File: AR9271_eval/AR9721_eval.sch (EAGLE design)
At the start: 135 parts, among them J1 UJ2-MIBH2-4-SMT-TR, J3 HTST-110-01-XX-DV, J7 132134-15, J8 132134-15, U1 U-ATHEROS-AR9271, U2 AT24C04C-XHM-T, U3 LT3080EQPBF, U4 LT3080EQPBF, U5 LT3080EQPBF, U6 LT3080EQPBF, Y1 ECS-400-10-36-CKY-TR

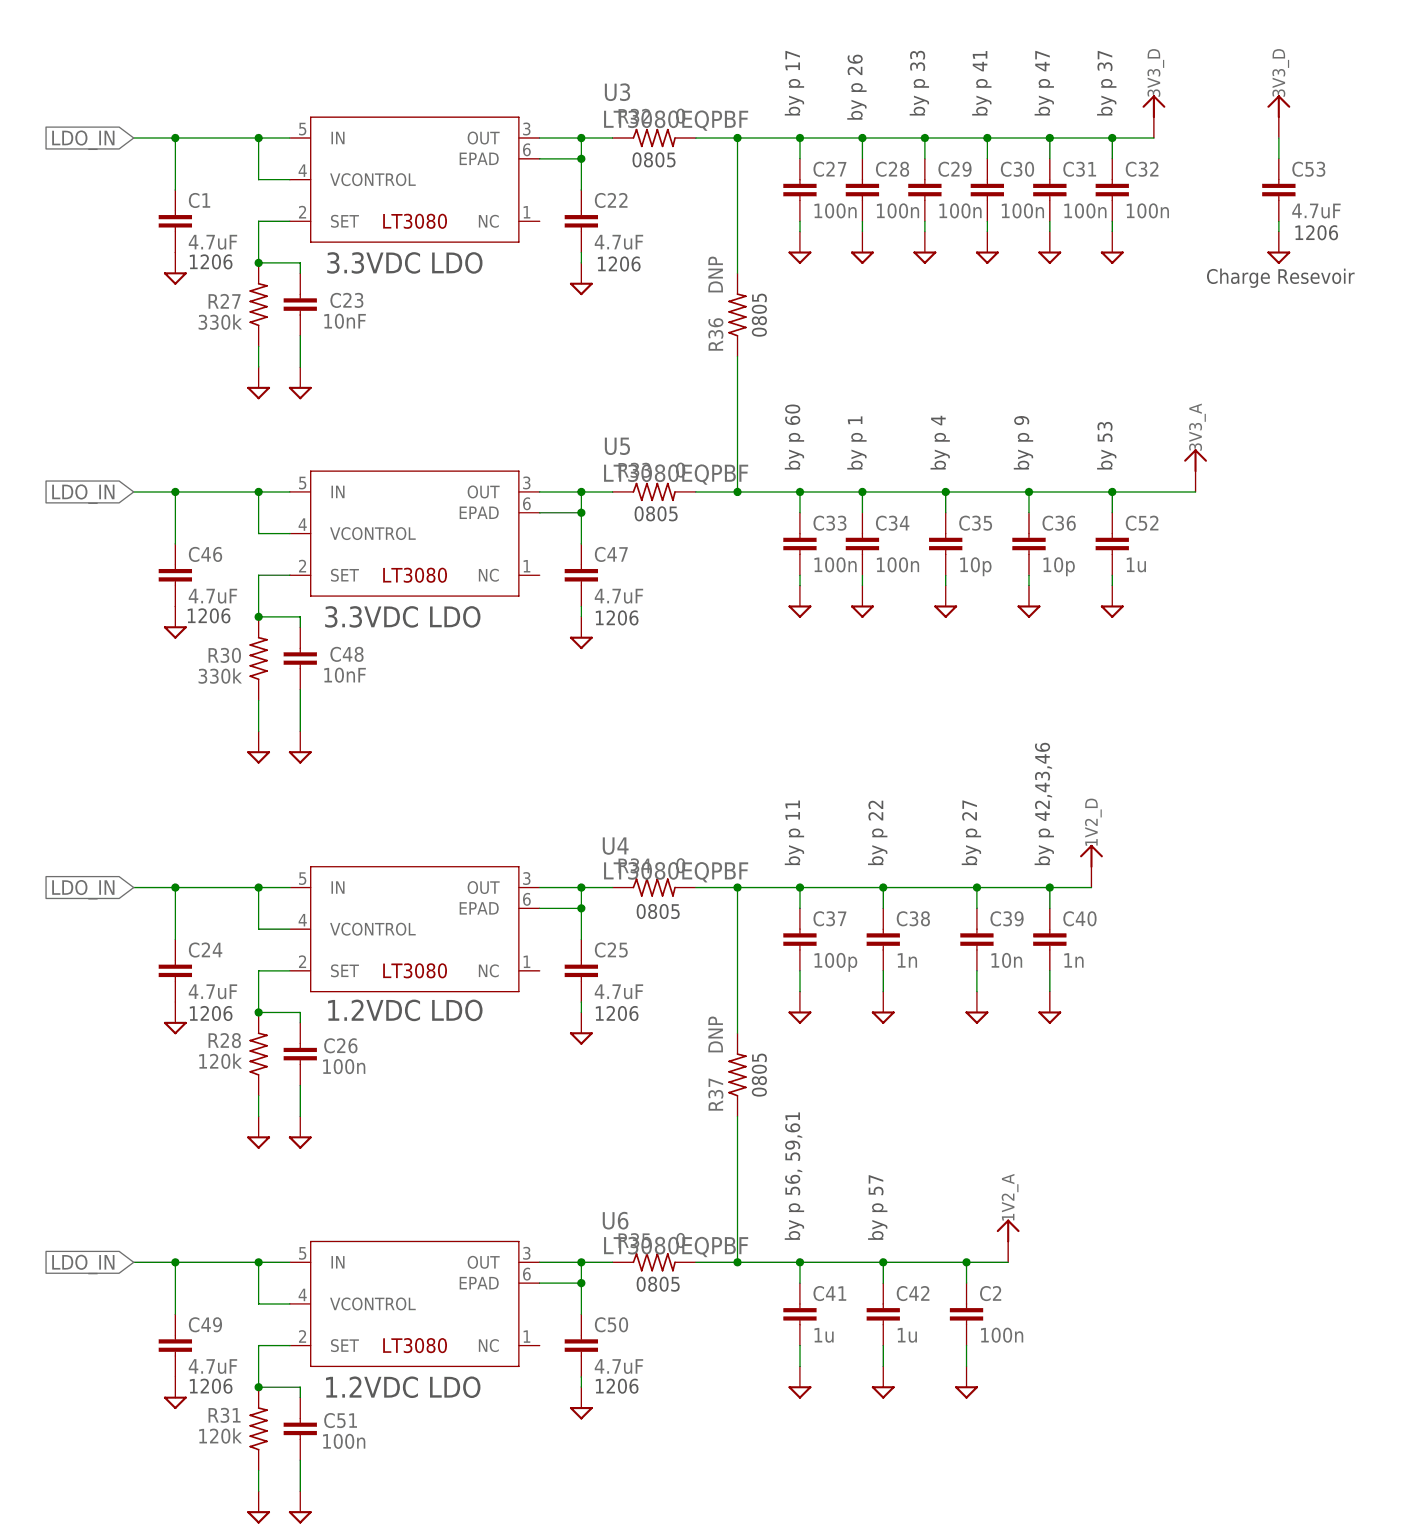
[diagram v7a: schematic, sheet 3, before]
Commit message: Fixed comments on JP4 and moved some names/values around after talking with Glenn.
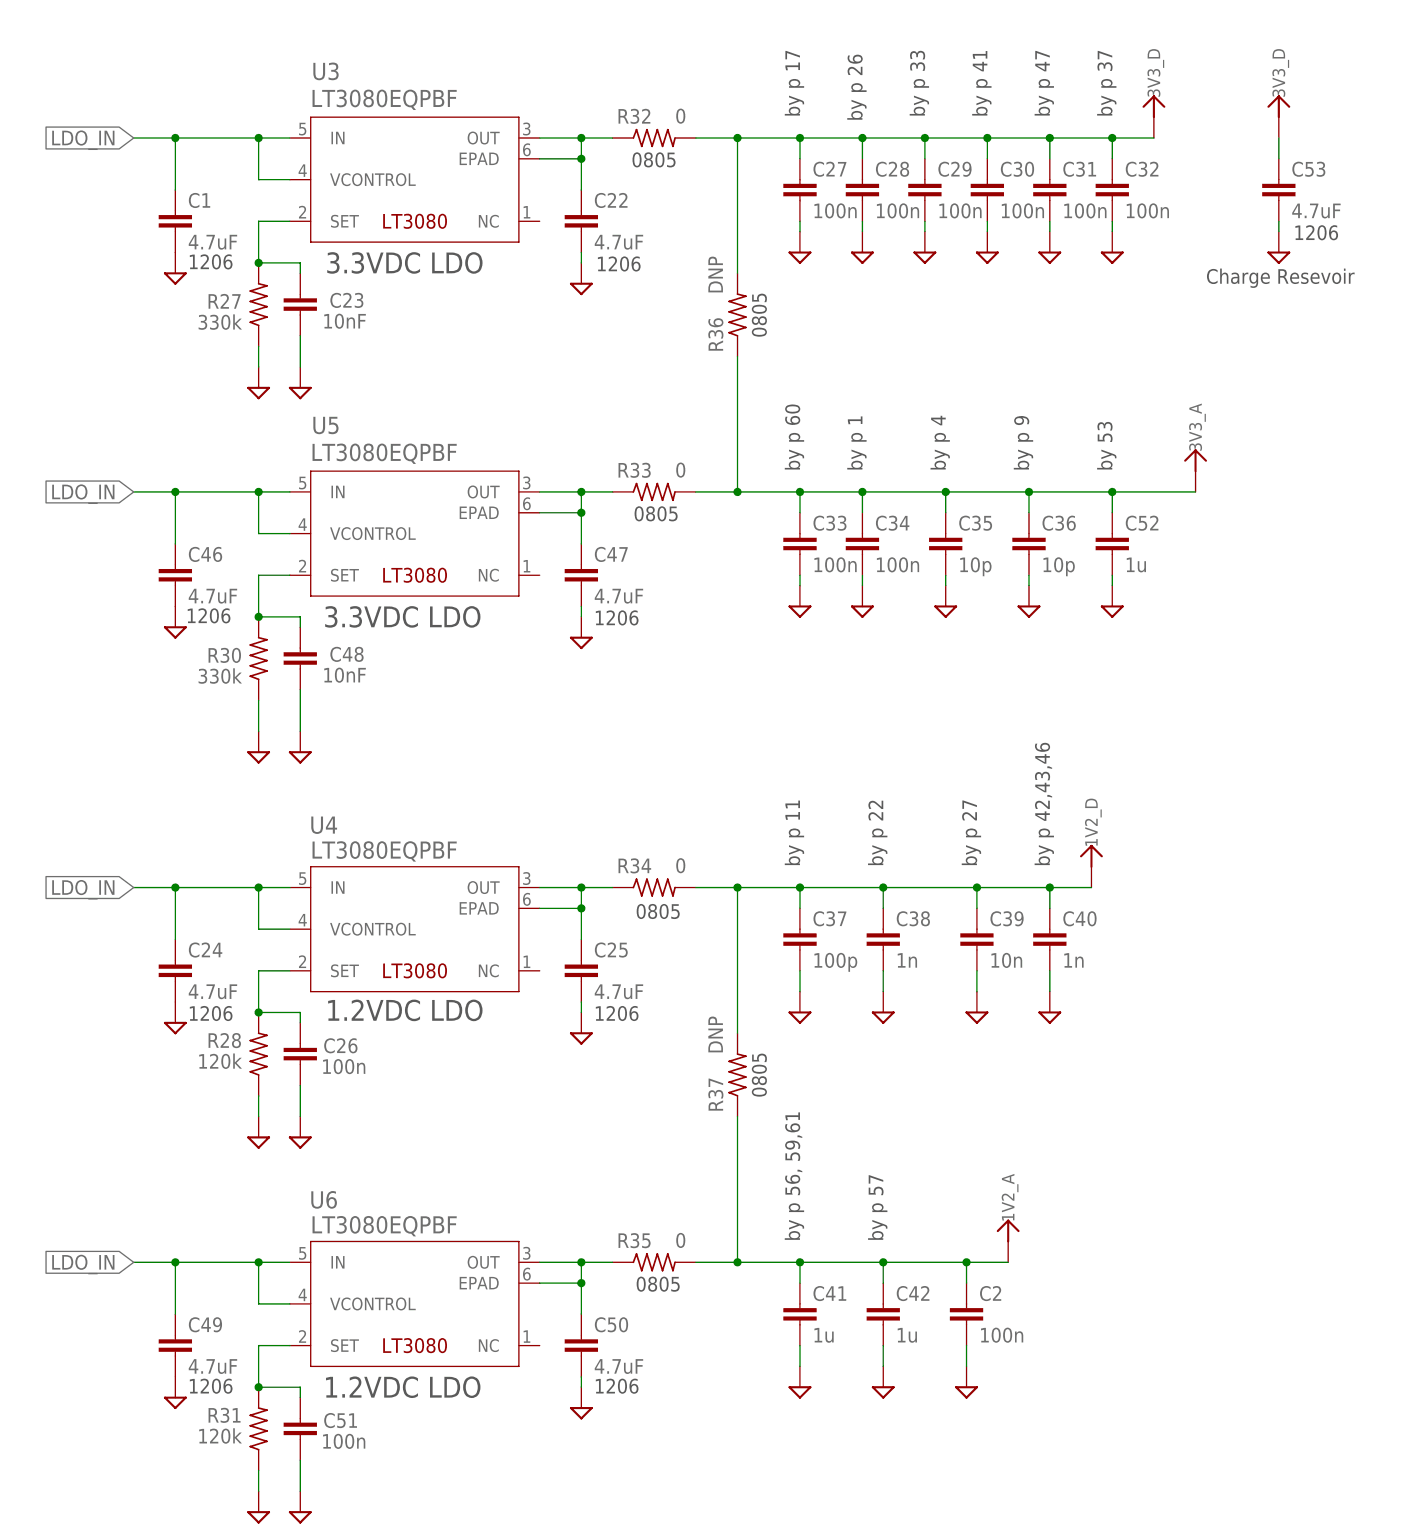
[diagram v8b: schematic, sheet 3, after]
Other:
- note added: "To use USB power for LDO input, connect connect Pin 5 to Pin 6 with jumper clip."
- note added: "To use lab supply, connect +5VDC to Pin 3 and Ground to Pin 7 or 8. Connect Pin 4 to Pin 5 with jumper clip."
- note removed: "To use USB for LDO input, connect connect Pin 3 to Pin 4 with jumper clip."
- note removed: "To use lab supply, connect +5VDC to Pin 6 and Ground to Pin 7 or 8. Connect Pin 5 to Pin 4 with jumper clip."
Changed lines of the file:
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@@
 <setting verticaltext="up"/>
 </settings>
-<grid distance="0.05" unitdist="inch" unit="inch" style="lines" multiple="2" display="no" altdistance="0.01" altunitdist="inch" altunit="inch"/>
+<grid distance="0.1" unitdist="inch" unit="inch" style="lines" multiple="1" display="no" altdistance="0.01" altunitdist="inch" altunit="inch"/>
 <layers>
 <layer number="1" name="Top" color="4" fill="1" visible="no" active="no"/>
@@
 <text x="86.106" y="216.408" size="1.778" layer="97">Ground</text>
 <text x="82.296" y="213.868" size="1.778" layer="97">Lab Supply</text>
-<text x="44.45" y="214.63" size="1.27" layer="97">To use USB for LDO input, connect
-connect Pin 3 to Pin 4 with jumper clip.</text>
-<text x="44.45" y="206.502" size="1.27" layer="97">To use lab supply, connect +5VDC to Pin 6
- and Ground to Pin 7 or 8. Connect Pin 5 to
- Pin 4 with jumper clip.</text>
+<text x="44.45" y="214.63" size="1.27" layer="97">To use USB power for LDO input, connect
+connect Pin 5 to Pin 6 with jumper clip.</text>
+<text x="44.45" y="206.502" size="1.27" layer="97">To use lab supply, connect +5VDC to Pin 3
+ and Ground to Pin 7 or 8. Connect Pin 4 to
+ Pin 5 with jumper clip.</text>
 <text x="302.768" y="132.588" size="1.778" layer="97">Serial Port</text>
 <text x="375.158" y="112.268" size="1.778" layer="97">GPIOs (8)</text>
@@
 </instance>
 <instance part="U3" gate="A" x="69.85" y="182.88" smashed="yes">
-<attribute name="NAME" x="92.8116" y="192.5066" size="2.0828" layer="95" ratio="6" rot="SR0"/>
-<attribute name="VALUE" x="92.6846" y="189.2046" size="2.0828" layer="96" ratio="6" rot="SR0"/>
+<attribute name="NAME" x="57.2516" y="195.0466" size="2.0828" layer="95" ratio="6" rot="SR0"/>
+<attribute name="VALUE" x="57.1246" y="191.7446" size="2.0828" layer="96" ratio="6" rot="SR0"/>
 </instance>
 <instance part="C1" gate="G$1" x="40.64" y="179.07" smashed="yes">
@@
 </instance>
 <instance part="U4" gate="A" x="69.85" y="91.44" smashed="yes">
-<attribute name="NAME" x="92.5576" y="100.5586" size="2.0828" layer="95" ratio="6" rot="SR0"/>
-<attribute name="VALUE" x="92.6846" y="97.5106" size="2.0828" layer="96" ratio="6" rot="SR0"/>
+<attribute name="NAME" x="56.9976" y="103.0986" size="2.0828" layer="95" ratio="6" rot="SR0"/>
+<attribute name="VALUE" x="57.1246" y="100.0506" size="2.0828" layer="96" ratio="6" rot="SR0"/>
 </instance>
 <instance part="C24" gate="G$1" x="40.64" y="87.63" smashed="yes">
@@
 <instance part="SUPPLY66" gate="GND" x="127" y="35.56" smashed="yes"/>
 <instance part="U5" gate="A" x="69.85" y="139.7" smashed="yes">
-<attribute name="NAME" x="92.8116" y="149.3266" size="2.0828" layer="95" ratio="6" rot="SR0"/>
-<attribute name="VALUE" x="92.6846" y="146.0246" size="2.0828" layer="96" ratio="6" rot="SR0"/>
+<attribute name="NAME" x="57.2516" y="151.8666" size="2.0828" layer="95" ratio="6" rot="SR0"/>
+<attribute name="VALUE" x="57.1246" y="148.5646" size="2.0828" layer="96" ratio="6" rot="SR0"/>
 </instance>
 <instance part="C46" gate="G$1" x="40.64" y="135.89" smashed="yes">
@@
 </instance>
 <instance part="U6" gate="A" x="69.85" y="45.72" smashed="yes">
-<attribute name="NAME" x="92.5576" y="54.8386" size="2.0828" layer="95" ratio="6" rot="SR0"/>
-<attribute name="VALUE" x="92.6846" y="51.7906" size="2.0828" layer="96" ratio="6" rot="SR0"/>
+<attribute name="NAME" x="56.9976" y="57.3786" size="2.0828" layer="95" ratio="6" rot="SR0"/>
+<attribute name="VALUE" x="57.1246" y="54.3306" size="2.0828" layer="96" ratio="6" rot="SR0"/>
 </instance>
 <instance part="C49" gate="G$1" x="40.64" y="41.91" smashed="yes">
